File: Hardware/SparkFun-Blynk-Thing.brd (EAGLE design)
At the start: 50 x 41.9 mm, 100 parts, among them IC1 OPAMP-DUALU, Q1 2.5A/30V, Q2 MMBT2222A, Q3 MMBT2222A, U1 MCP73831, U2 ESP8266, U3 AP2112K-3.3V, U4 FT231XS-U, U5 W25Q32FVSS, U6 SI7021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

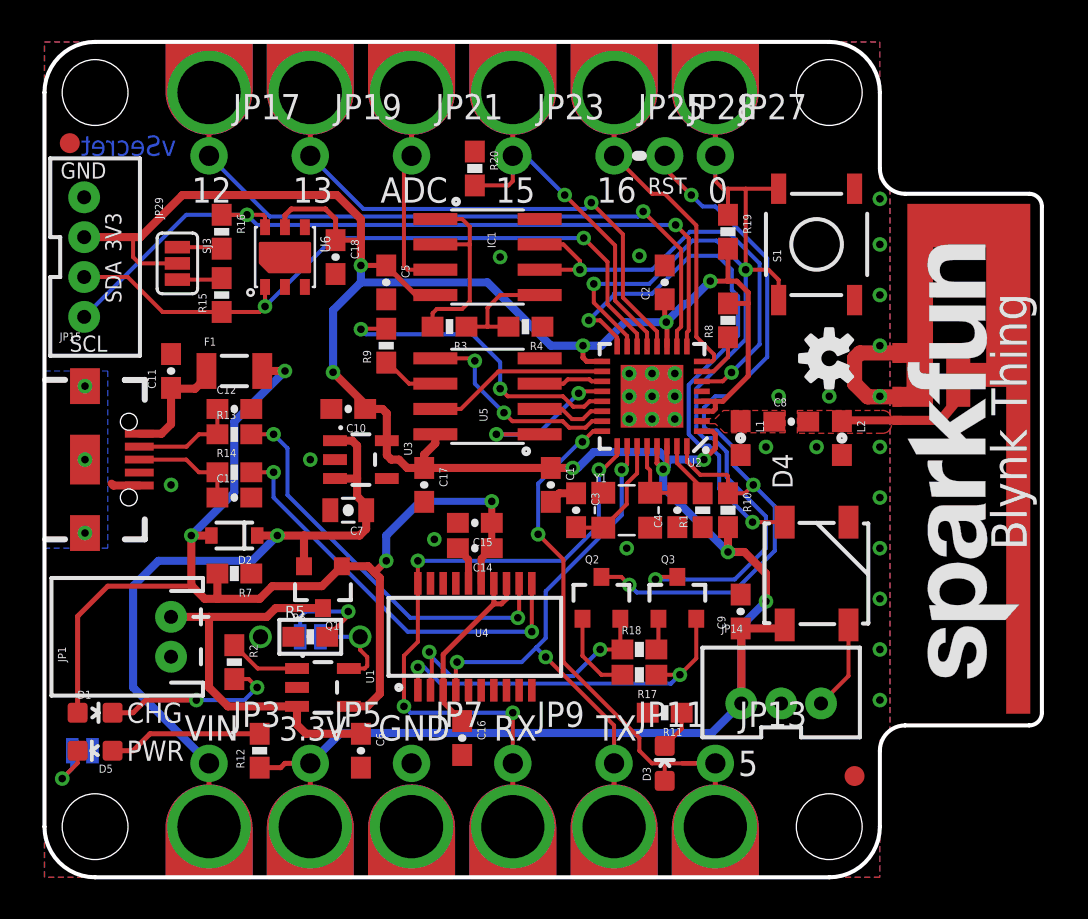
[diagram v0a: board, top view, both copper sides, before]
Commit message: Re-configuring the I2C connector.
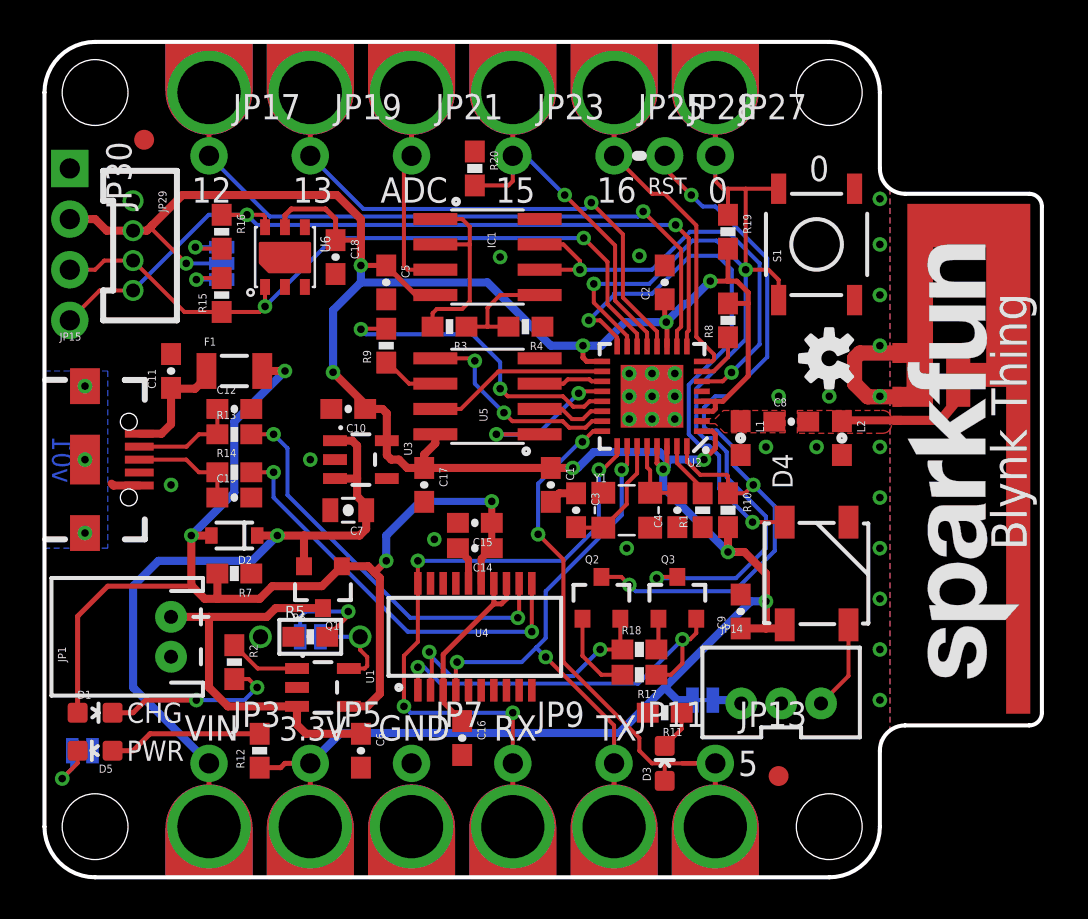
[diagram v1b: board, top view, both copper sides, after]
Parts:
- added JP30: (no value), SparkFun-Connectors:1X04_NO_SILK
- added SJ4: (no value), SparkFun-Passives:PAD-JUMPER-3-3OF3_NC_BY_TRACE_YES_SILK_FULL_BOX
- D4: value (none) -> WS2812
- JP29: device SparkFun-Connectors:JST-4-PTH-VERT -> SparkFun-Connectors:1X04-1.5MM_JST
- SJ3: value (none) -> WS2812-VCC; device SparkFun-Passives:PAD-JUMPER-3-NC_BY_PASTE_YES_SILK_FULL_BOX -> SparkFun-Passives:PAD-JUMPER-2-NC_BY_TRACE_YES_SILK
- moved SJ3 34.3 mm to (33.0, 8.89), flipped to the bottom, turned to 0 degrees
- moved FID1 3.81 mm to (36.8, 5.08)
- moved FID2 3.73 mm to (5.00, 37.0)
- moved JP29 3.41 mm to (4.45, 33.9)
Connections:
- new net N$19: JP14.1, SJ3.1
- net 14/SCL: now also JP30.4
- net 2/SDA: now also JP30.3
- net GND: now also JP30.1
- net N$11: now also SJ4.3; no longer SJ3.3
- net N$13: now also SJ4.1; no longer SJ3.1
- net VCC: now also JP30.2, SJ4.2; no longer JP14.1
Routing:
- net N$19: track 0.00 -> 1.50 mm
- net 2/SDA: track 34.8 -> 36.1 mm
- net VCC: track 154.8 -> 153.7 mm, vias 10 -> 11
- net DTR: track 19.2 -> 20.0 mm
- net 14/SCL: track 41.1 -> 41.9 mm
- net N$13: track 2.25 -> 2.67 mm, vias 0 -> 1
- net N$11: track 2.25 -> 2.57 mm, vias 0 -> 1
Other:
- board text added: "CHG RES"
- board text added: "I2C PU"
- board text added: "PWR LED"
- board text added: "WS2812 VCC"
- board text added: "v01"
- board text removed: "vSecret"

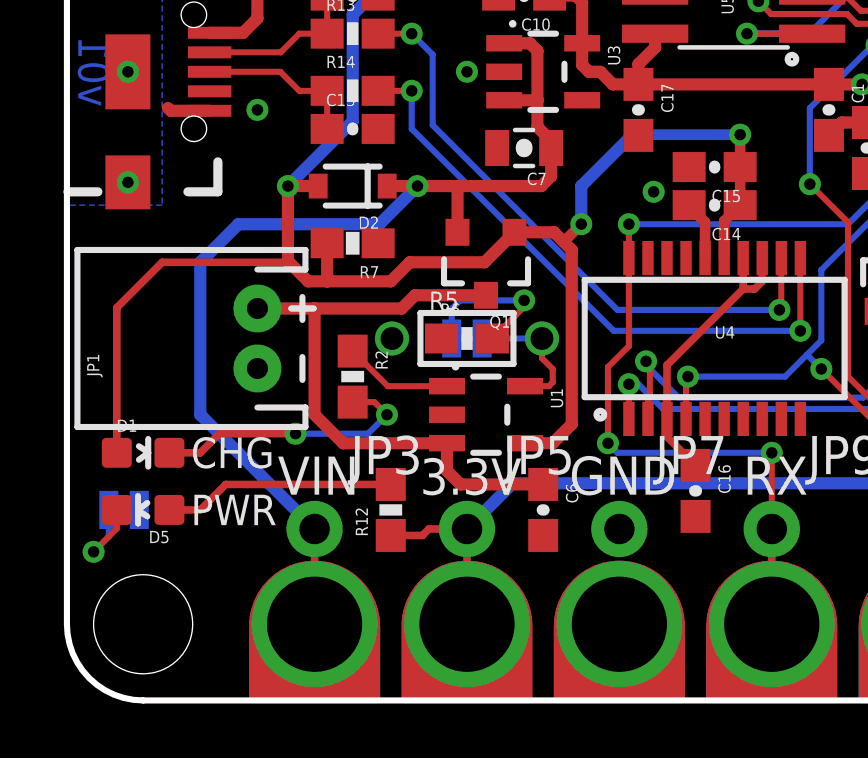
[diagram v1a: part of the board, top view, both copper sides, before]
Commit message: Schematic cleanup, adding decoupling cap to batt charger
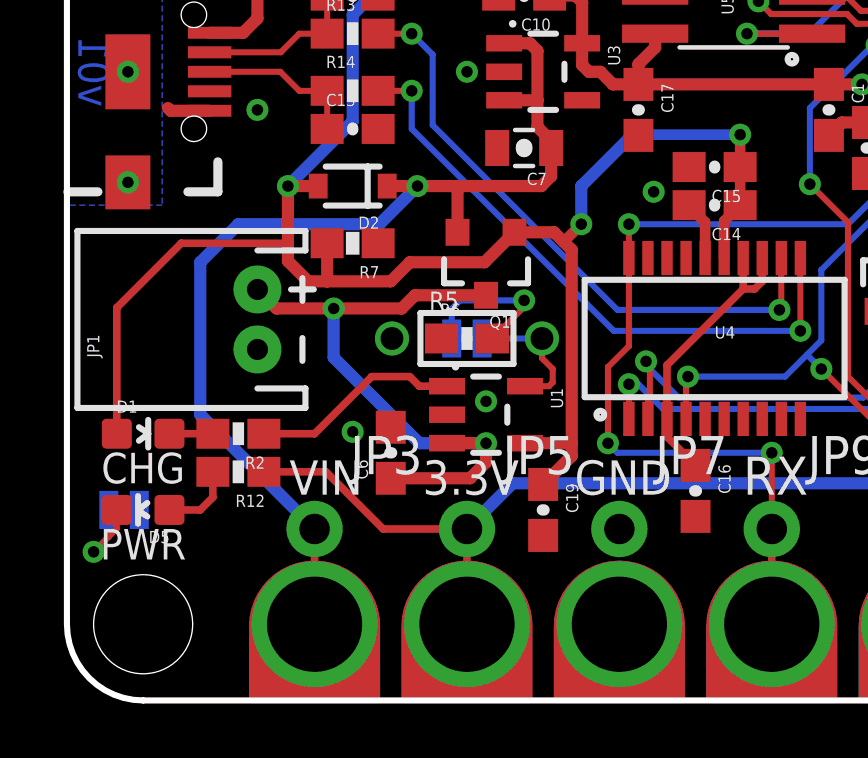
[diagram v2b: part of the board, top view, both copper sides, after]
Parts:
- added C19: 4.7uF, SparkFun-Capacitors:0603-CAP
- moved C6 5.43 mm to (10.8, 8.26), turned to 90 degrees
- moved R12 5.24 mm to (5.71, 7.62), turned to 180 degrees
- moved R2 4.26 mm to (5.71, 8.89), turned to 180 degrees
- moved D1 0.63 mm to (2.54, 8.89)
- moved JP1 0.63 mm to (6.35, 12.7)
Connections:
- net VBAT renamed V_BATT
- removed net RXLED: U4.17
- removed net TXLED: U4.10
- net GND: now also C19.2
- net V_USB: now also C19.1
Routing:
- net N$17: track 9.09 -> 1.45 mm, vias 2 -> 0
- net N$10: track 7.73 -> 2.47 mm
- net VCC: track 153.7 -> 158.6 mm
- net N$9: track 3.63 -> 7.03 mm
- net V_USB: track 58.0 -> 59.8 mm
- net V_BATT: track 20.5 -> 21.3 mm, vias 0 -> 2
- net GND: vias 30 -> 32

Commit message: Schematic clean-up and some PROD_ID's
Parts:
- IC1: value OPAMP-DUALU -> LMV358
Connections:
- net D+: now also JP15.D+; no longer JP15.D+1
- net D-: now also JP15.D-; no longer JP15.D-1
- net GND: now also JP15.GND; no longer JP15.GND1
- net VUSB: now also JP15.VBUS; no longer JP15.VBUS1
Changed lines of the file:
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@@
 <element name="JP4" library="blynk-thing-temp" package="1X01_ALLIGATOR_3MM_HALF" value="" x="13.335" y="2.54" rot="R180"/>
 <element name="JP6" library="blynk-thing-temp" package="1X01_ALLIGATOR_3MM_HALF" value="" x="18.415" y="2.54" rot="R180"/>
-<element name="JP29" library="SparkFun-Connectors" package="1X04-1.5MM_JST" value="" x="4.445" y="33.94" rot="R270"/>
+<element name="JP29" library="SparkFun-Connectors" package="1X04-1.5MM_JST" value="" x="4.445" y="33.94" rot="R270">
+<attribute name="PROD_ID" value="CONN-12477" x="4.445" y="33.94" size="1.778" layer="27" rot="R270" display="off"/>
+</element>
 <element name="D4" library="SparkFun-LED" package="WS2812B" value="WS2812" x="38.735" y="15.24" rot="R90">
 <attribute name="PROD_ID" value="DIO-12503" x="38.735" y="15.24" size="1.778" layer="27" font="vector" ratio="15" rot="R90" display="off"/>
 </element>
-<element name="JP14" library="SparkFun-Connectors" package="JST-3-PTH-VERT" value="" x="36.957" y="9.271"/>
+<element name="JP14" library="SparkFun-Connectors" package="JST-3-PTH-VERT" value="" x="36.957" y="9.271">
+<attribute name="PROD_ID" value="TBD" x="36.957" y="9.271" size="1.778" layer="27" display="off"/>
+</element>
 <element name="U6" library="SparkFun-Sensors" package="SI7021" value="SI7021" x="12.065" y="31.115" rot="R270">
 <attribute name="PROD_ID" value="IC-13093" x="12.065" y="31.115" size="1.778" layer="27" ratio="15" rot="R270" display="off"/>
@@
 <attribute name="PROD_ID" value="CAP-00810" x="34.925" y="13.335" size="1.778" layer="27" ratio="15" rot="R90" display="off"/>
 </element>
-<element name="IC1" library="SparkFun-AnalogIC" package="SO08" value="OPAMP-DUALU" x="22.225" y="31.115" rot="R270"/>
+<element name="IC1" library="SparkFun-AnalogIC" package="SO08" value="LMV358" x="22.225" y="31.115" rot="R270">
+<attribute name="PROD_ID" value="IC-09657" x="22.225" y="31.115" size="1.778" layer="27" rot="R270" display="off"/>
+</element>
 <element name="R3" library="SparkFun-Resistors" package="0603-RES" value="22K" x="20.32" y="27.6225" rot="R180">
 <attribute name="PROD_ID" value="RES-07853" x="20.32" y="27.6225" size="1.778" layer="27" ratio="15" rot="R180" display="off"/>
@@
 <contactref element="R20" pad="1"/>
 <contactref element="C11" pad="2"/>
-<contactref element="JP15" pad="GND1"/>
+<contactref element="JP15" pad="GND"/>
 <contactref element="C13" pad="2"/>
 <contactref element="C12" pad="2"/>
@@
 <contactref element="R13" pad="1"/>
 <contactref element="C12" pad="1"/>
-<contactref element="JP15" pad="D-1"/>
+<contactref element="JP15" pad="D-"/>
 <wire x1="8.675" y1="22.225" x2="8.675" y2="23.495" width="0.2032" layer="1"/>
 <wire x1="4.757" y1="21.605" x2="7.127" y2="21.605" width="0.2032" layer="1"/>
@@
 <contactref element="R14" pad="1"/>
 <contactref element="C13" pad="1"/>
-<contactref element="JP15" pad="D+1"/>
+<contactref element="JP15" pad="D+"/>
 <wire x1="8.675" y1="19.05" x2="8.675" y2="20.32" width="0.2032" layer="1"/>
 <wire x1="4.757" y1="20.955" x2="7.112" y2="20.955" width="0.2032" layer="1"/>
@@
 <contactref element="C11" pad="1"/>
 <contactref element="F1" pad="1"/>
-<contactref element="JP15" pad="VBUS1"/>
+<contactref element="JP15" pad="VBUS"/>
 <wire x1="4.757" y1="22.255" x2="5.872" y2="22.255" width="0.4064" layer="1"/>
 <wire x1="5.872" y1="22.255" x2="6.35" y2="22.733" width="0.4064" layer="1"/>

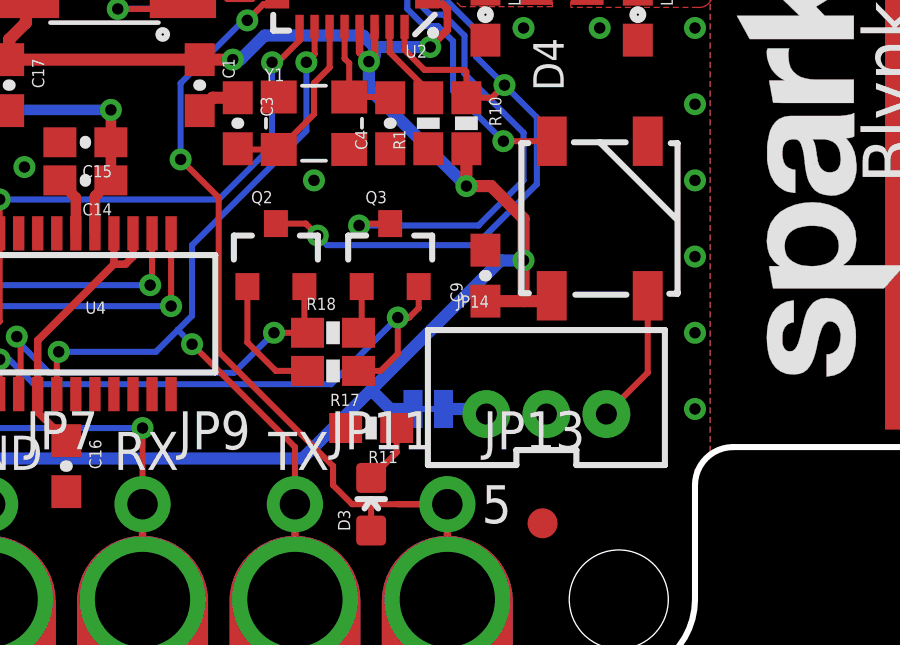
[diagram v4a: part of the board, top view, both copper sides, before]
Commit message: Moving WS2812-VCC jumper.
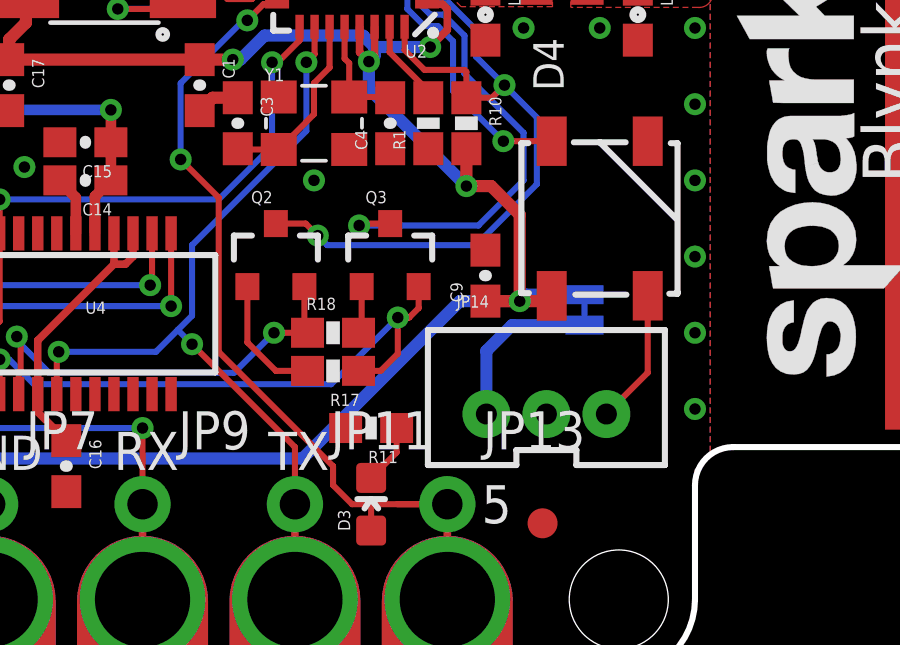
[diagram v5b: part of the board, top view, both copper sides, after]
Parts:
- moved SJ3 6.17 mm to (38.2, 12.2), turned to 90 degrees
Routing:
- net N$19: track 1.50 -> 5.73 mm
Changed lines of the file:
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@@
 <layer number="47" name="Measures" color="7" fill="1" visible="no" active="yes"/>
 <layer number="48" name="Document" color="7" fill="1" visible="no" active="yes"/>
-<layer number="49" name="Reference" color="7" fill="1" visible="no" active="yes"/>
+<layer number="49" name="Reference" color="7" fill="1" visible="yes" active="yes"/>
 <layer number="50" name="dxf" color="7" fill="1" visible="no" active="no"/>
 <layer number="51" name="tDocu" color="6" fill="1" visible="yes" active="yes"/>
@@
 <text x="13.208" y="6.858" size="1.2065" layer="22" ratio="15" rot="MR0" align="bottom-center">3.3V</text>
 <text x="8.128" y="6.858" size="1.27" layer="22" ratio="15" rot="MR0" align="bottom-center">VIN</text>
-<text x="36.957" y="9.779" size="1.27" layer="22" font="vector" ratio="15" rot="MR90" align="center-left">GND</text>
-<text x="34.957" y="9.779" size="1.27" layer="22" font="vector" ratio="15" rot="MR90" align="center-left">3.3V</text>
-<text x="38.957" y="9.779" size="1.27" layer="22" font="vector" ratio="15" rot="MR90" align="center-left">DOUT</text>
 <wire x1="29.718" y1="36.195" x2="29.972" y2="36.195" width="0.508" layer="21"/>
 <wire x1="29.718" y1="36.195" x2="29.972" y2="36.195" width="0.508" layer="22"/>
@@
 <text x="38.862" y="34.925" size="1.27" layer="21" ratio="15" rot="R180" align="top-center">0</text>
 <text x="34.544" y="5.715" size="1.27" layer="22" ratio="15" rot="MR0" align="center-right">5</text>
-<text x="33.02" y="10.16" size="0.8128" layer="22" font="vector" ratio="15" rot="MR90" align="center-left">WS2812
+<text x="38.227" y="13.462" size="0.8128" layer="22" font="vector" ratio="15" rot="MR90" align="center-left">WS2812
 VCC</text>
 <wire x1="3.556" y1="35.56" x2="4.445" y2="33.909" width="0.2032" layer="22"/>
@@
 <wire x1="4.445" y1="29.464" x2="3.556" y2="27.94" width="0.2032" layer="22"/>
 <text x="2.54" y="8.255" size="1.016" layer="21" font="vector" ratio="15" rot="R180" align="bottom-center">CHG</text>
+<text x="36.957" y="7.62" size="0.889" layer="22" font="vector" ratio="15" rot="MR180" align="bottom-center">GND</text>
+<text x="34.83" y="9.779" size="0.889" layer="22" font="vector" ratio="15" rot="MR0" align="bottom-center">3.3V</text>
+<text x="39.084" y="9.779" size="0.889" layer="22" font="vector" ratio="15" rot="MR0" align="bottom-center">DOUT</text>
 </plain>
 <attributes>
@@
 <element name="JP3" library="SparkFun-Connectors" package="1X01_NO_SILK" value="" x="8.255" y="5.715"/>
 <element name="SJ4" library="SparkFun-Passives" package="PAD-JUMPER-3-3OF3_NC_BY_TRACE_YES_SILK_FULL_BOX" value="" x="8.89" y="30.7975" rot="MR270"/>
-<element name="SJ3" library="SparkFun-Passives" package="PAD-JUMPER-2-NC_BY_TRACE_YES_SILK" value="WS2812-VCC" x="33.02" y="8.89" rot="MR0"/>
+<element name="SJ3" library="SparkFun-Passives" package="PAD-JUMPER-2-NC_BY_TRACE_YES_SILK" value="WS2812-VCC" x="38.227" y="12.192" rot="MR90"/>
 <element name="JP30" library="SparkFun-Connectors" package="1X04_NO_SILK" value="" x="1.27" y="35.56" rot="R270"/>
 <element name="C19" library="SparkFun-Capacitors" package="0603-CAP" value="4.7uF" x="15.875" y="6.35" rot="R270">
@@
 <wire x1="28.829" y1="7.239" x2="14.859" y2="7.239" width="0.4064" layer="16"/>
 <wire x1="34.957" y1="12.453" x2="34.925" y2="12.485" width="0.4064" layer="1"/>
-<wire x1="36.195" y1="12.485" x2="36.957" y2="12.485" width="0.4064" layer="1"/>
 <wire x1="36.957" y1="12.485" x2="37.135" y2="12.663" width="0.4064" layer="1"/>
 <wire x1="34.29" y1="17.565" x2="34.29" y2="16.3195" width="0.4064" layer="1"/>
@@
 <wire x1="14.859" y1="7.239" x2="13.335" y2="5.715" width="0.4064" layer="16"/>
 <wire x1="13.335" y1="2.54" x2="13.335" y2="5.715" width="0.254" layer="1"/>
-<via x="36.195" y="13.843" extent="1-16" drill="0.381"/>
 <wire x1="34.29" y1="16.3195" x2="35.1155" y2="16.3195" width="0.4064" layer="1"/>
-<wire x1="35.1155" y1="16.3195" x2="36.195" y2="15.24" width="0.4064" layer="1"/>
-<wire x1="36.195" y1="15.24" x2="36.195" y2="13.843" width="0.4064" layer="1"/>
 <via x="14.478" y="25.3365" extent="1-16" drill="0.381"/>
 <via x="15.875" y="30.695" extent="1-16" drill="0.381"/>
@@
 <via x="7.112" y="30.7975" extent="1-16" drill="0.381"/>
 <contactref element="SJ3" pad="2"/>
-<wire x1="36.195" y1="13.843" x2="36.195" y2="12.485" width="0.4064" layer="1"/>
-<wire x1="36.195" y1="12.485" x2="34.925" y2="12.485" width="0.4064" layer="1"/>
-<wire x1="31.115" y1="9.525" x2="28.829" y2="7.239" width="0.4064" layer="16"/>
-<wire x1="32.512" y1="8.89" x2="31.75" y2="8.89" width="0.4064" layer="16"/>
-<wire x1="31.75" y1="8.89" x2="31.115" y2="9.525" width="0.4064" layer="16"/>
-<wire x1="31.115" y1="9.525" x2="35.433" y2="13.843" width="0.4064" layer="16"/>
-<wire x1="35.433" y1="13.843" x2="36.195" y2="13.843" width="0.4064" layer="16"/>
+<wire x1="36.957" y1="12.485" x2="36.068" y2="12.485" width="0.4064" layer="1"/>
+<wire x1="36.068" y1="12.485" x2="34.925" y2="12.485" width="0.4064" layer="1"/>
+<wire x1="28.829" y1="7.239" x2="34.075" y2="12.485" width="0.4064" layer="16"/>
 <contactref element="JP30" pad="2"/>
 <wire x1="4.445" y1="32.44" x2="5.135" y2="32.44" width="0.4064" layer="1"/>
@@
 <wire x1="6.565" y1="7.62" x2="8.636" y2="7.62" width="0.254" layer="1"/>
 <wire x1="8.636" y1="7.62" x2="10.541" y2="5.715" width="0.254" layer="1"/>
+<wire x1="34.075" y1="12.485" x2="36.068" y2="12.485" width="0.4064" layer="16"/>
+<via x="36.068" y="12.485" extent="1-16" drill="0.381"/>
+<wire x1="36.068" y1="12.485" x2="36.068" y2="15.367" width="0.4064" layer="1"/>
+<wire x1="36.068" y1="15.367" x2="35.1155" y2="16.3195" width="0.4064" layer="1"/>
+<wire x1="38.227" y1="12.7" x2="36.283" y2="12.7" width="0.4064" layer="16"/>
+<wire x1="36.283" y1="12.7" x2="36.068" y2="12.485" width="0.4064" layer="16"/>
 </signal>
 <signal name="GND">
@@
 <contactref element="JP14" pad="1"/>
 <contactref element="SJ3" pad="1"/>
-<wire x1="33.528" y1="8.89" x2="34.788" y2="8.89" width="0.4064" layer="16"/>
-<wire x1="34.788" y1="8.89" x2="34.957" y2="8.721" width="0.4064" layer="16"/>
+<wire x1="38.227" y1="11.684" x2="35.814" y2="11.684" width="0.4064" layer="16"/>
+<wire x1="34.957" y1="8.721" x2="34.957" y2="10.827" width="0.4064" layer="16"/>
+<wire x1="34.957" y1="10.827" x2="35.814" y2="11.684" width="0.4064" layer="16"/>
 </signal>
 </signals>

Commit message: Updating 32M Flash package.
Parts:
- U5: device blynk-thing-temp:SO08 -> blynk-thing-temp:SOIC-8
- moved U3 1.27 mm to (14.6, 21.0)
- moved C17 0.90 mm to (18.4, 19.1)
- moved R9 0.90 mm to (16.5, 26.0)
- moved U5 0.90 mm to (21.6, 23.5)
- moved C10 0.63 mm to (14.6, 23.5)
- moved C7 0.63 mm to (14.6, 18.4)
- moved C1 0.63 mm to (25.4, 19.1)
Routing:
- net SD_CS0: track 9.96 -> 7.37 mm
- net SD_SI: track 10.6 -> 12.8 mm
- net SD_CLK0: track 15.9 -> 14.2 mm
- net SD_!HD!: track 9.15 -> 10.7 mm
- net VCC: track 158.5 -> 159.2 mm
- net SD_!WP!: track 4.08 -> 3.45 mm
